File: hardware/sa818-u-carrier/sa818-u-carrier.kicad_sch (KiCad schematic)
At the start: 9 parts, among them J13 Conn_Coaxial, J14 Power/Audio, J15 Control/Data, J16 Conn_01x03_Pin, J17 Conn_01x03_Pin, U9 SA818V

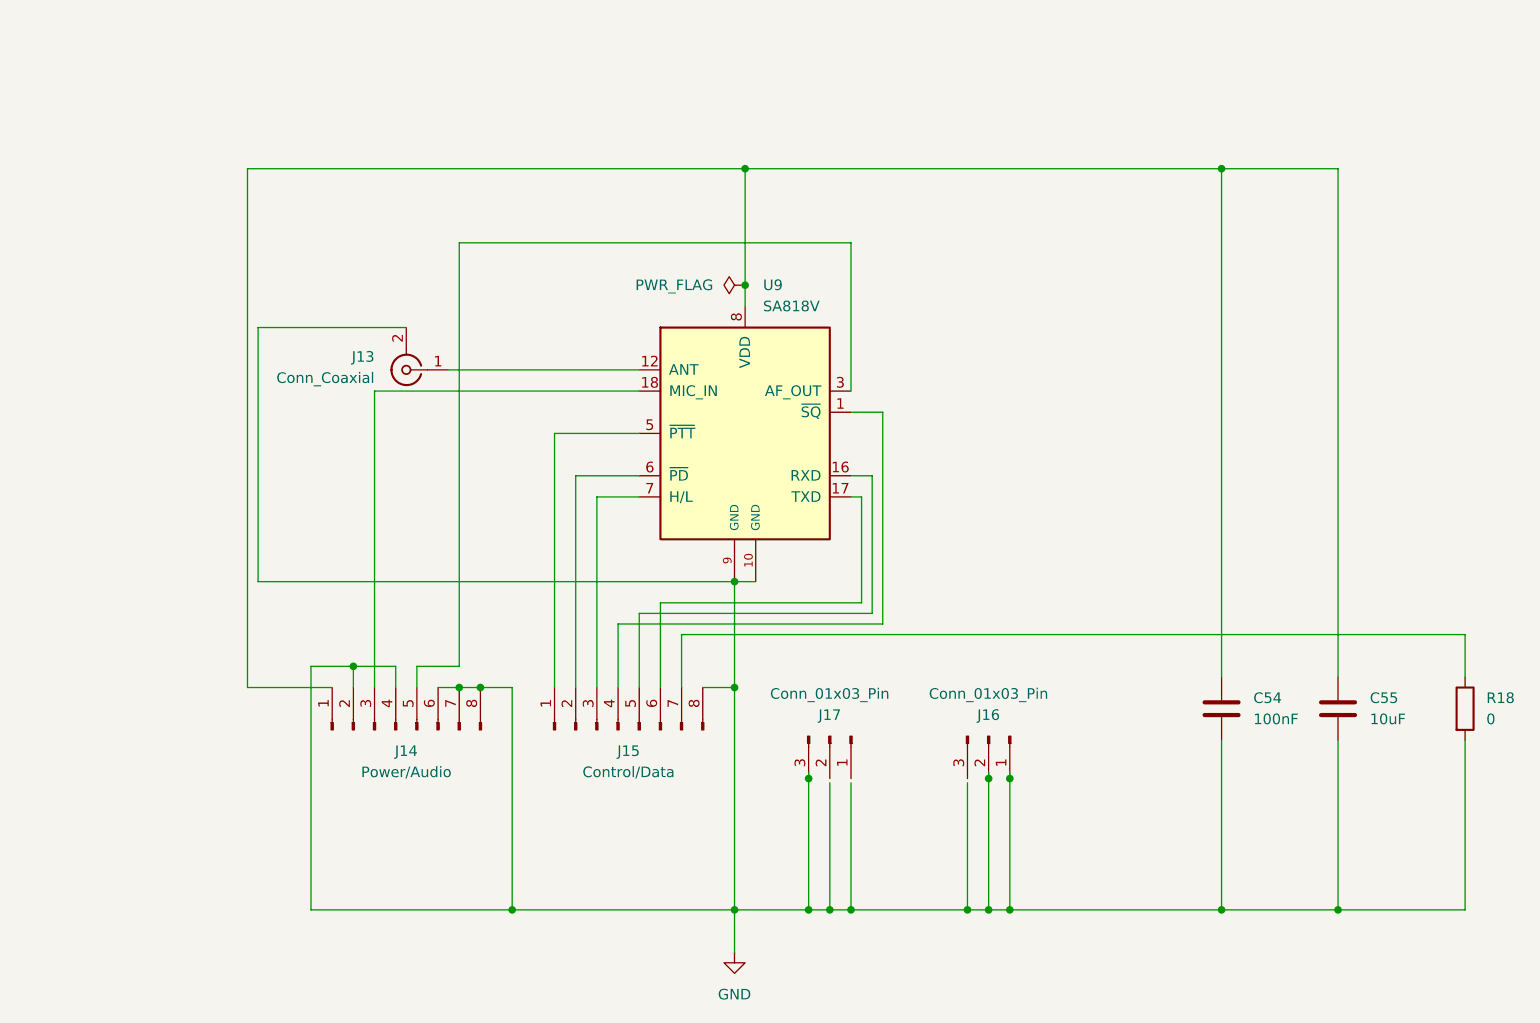
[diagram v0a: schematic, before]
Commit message: add footprints and break carrier boards out into standalone projects
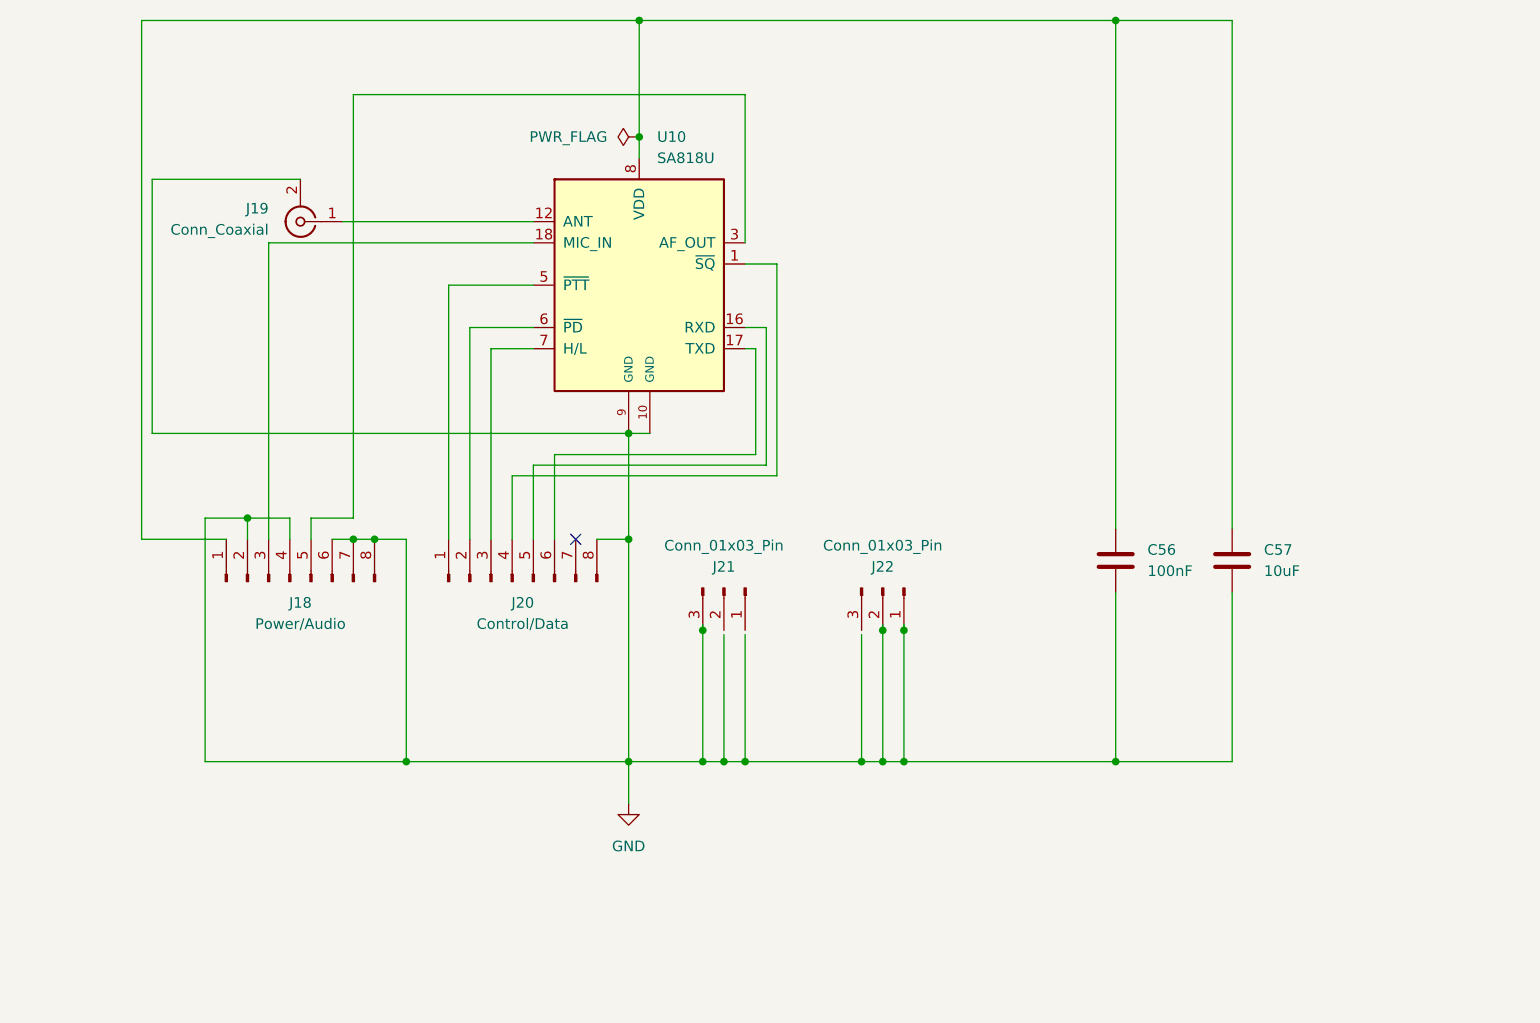
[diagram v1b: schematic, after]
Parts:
- removed C54: 100nF, Capacitor_SMD:C_0402_1005Metric, symbol Device:C
- removed C55: 10uF, Capacitor_SMD:C_0603_1608Metric, symbol Device:C
- removed J13: Conn_Coaxial, Connector_Coaxial:SMA_Amphenol_132289_EdgeMount, symbol Connector:Conn_Coaxial
- removed J14: Power/Audio, Connector_PinHeader_2.54mm:PinHeader_1x08_P2.54mm_Vertical, symbol Connector:Conn_01x08_Pin
- removed J15: Control/Data, Connector_PinHeader_2.54mm:PinHeader_1x08_P2.54mm_Vertical, symbol Connector:Conn_01x08_Pin
- removed J16, J17: Conn_01x03_Pin, Connector_PinHeader_2.54mm:PinHeader_1x03_P2.54mm_Vertical, symbol Connector:Conn_01x03_Pin
- removed R18: 0, Resistor_SMD:R_0402_1005Metric, symbol Device:R
- removed U9: SA818V, VHF_UHF_Modules:VHF_UHF_Module_generic, symbol VHF_UHF_Modules:SA818V
- added C56: 100nF, Capacitor_SMD:C_0402_1005Metric, symbol Device:C
- added C57: 10uF, Capacitor_SMD:C_0603_1608Metric, symbol Device:C
- added J18: Power/Audio, Connector_PinHeader_2.54mm:PinHeader_1x08_P2.54mm_Vertical, symbol Connector:Conn_01x08_Pin
- added J19: Conn_Coaxial, Connector_Coaxial:SMA_Amphenol_132289_EdgeMount, symbol Connector:Conn_Coaxial
- added J20: Control/Data, Connector_PinHeader_2.54mm:PinHeader_1x08_P2.54mm_Vertical, symbol Connector:Conn_01x08_Pin
- added J21, J22: Conn_01x03_Pin, Connector_PinHeader_2.54mm:PinHeader_1x03_P2.54mm_Vertical, symbol Connector:Conn_01x03_Pin
- added U10: SA818U, VHF_UHF_Modules:VHF_UHF_Module_generic, symbol VHF_UHF_Modules:SA818V
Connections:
- net GND: now also C56.2, C57.2, J18.2 (Pin_2), J18.4 (Pin_4), J18.6 (Pin_6), J18.7 (Pin_7), J18.8 (Pin_8), J19.2 (Ext), J20.8 (Pin_8), J21.3 (Pin_3), J22.1 (Pin_1), J22.2 (Pin_2), U10.10 (GND), U10.9 (GND)
- new net: J20.1 (Pin_1), U10.5 (~{PTT})
- new net: J20.2 (Pin_2), U10.6 (~{PD})
- new net: J20.3 (Pin_3), U10.7 (H/L)
- new net: J20.4 (Pin_4), U10.1 (~{SQ})
- new net: J20.5 (Pin_5), U10.16 (RXD)
- new net: J20.6 (Pin_6), U10.17 (TXD)
- new net: J19.1 (In), U10.12 (ANT)
- new net: J18.3 (Pin_3), U10.18 (MIC_IN)
- new net: J18.5 (Pin_5), U10.3 (AF_OUT)
- new net: C56.1, C57.1, J18.1 (Pin_1), U10.8 (VDD)
- no-connect marks 0 -> 1
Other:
- title: VHF RF Carrier Board -> UHF RF Carrier Board

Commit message: routing and component bug fixes
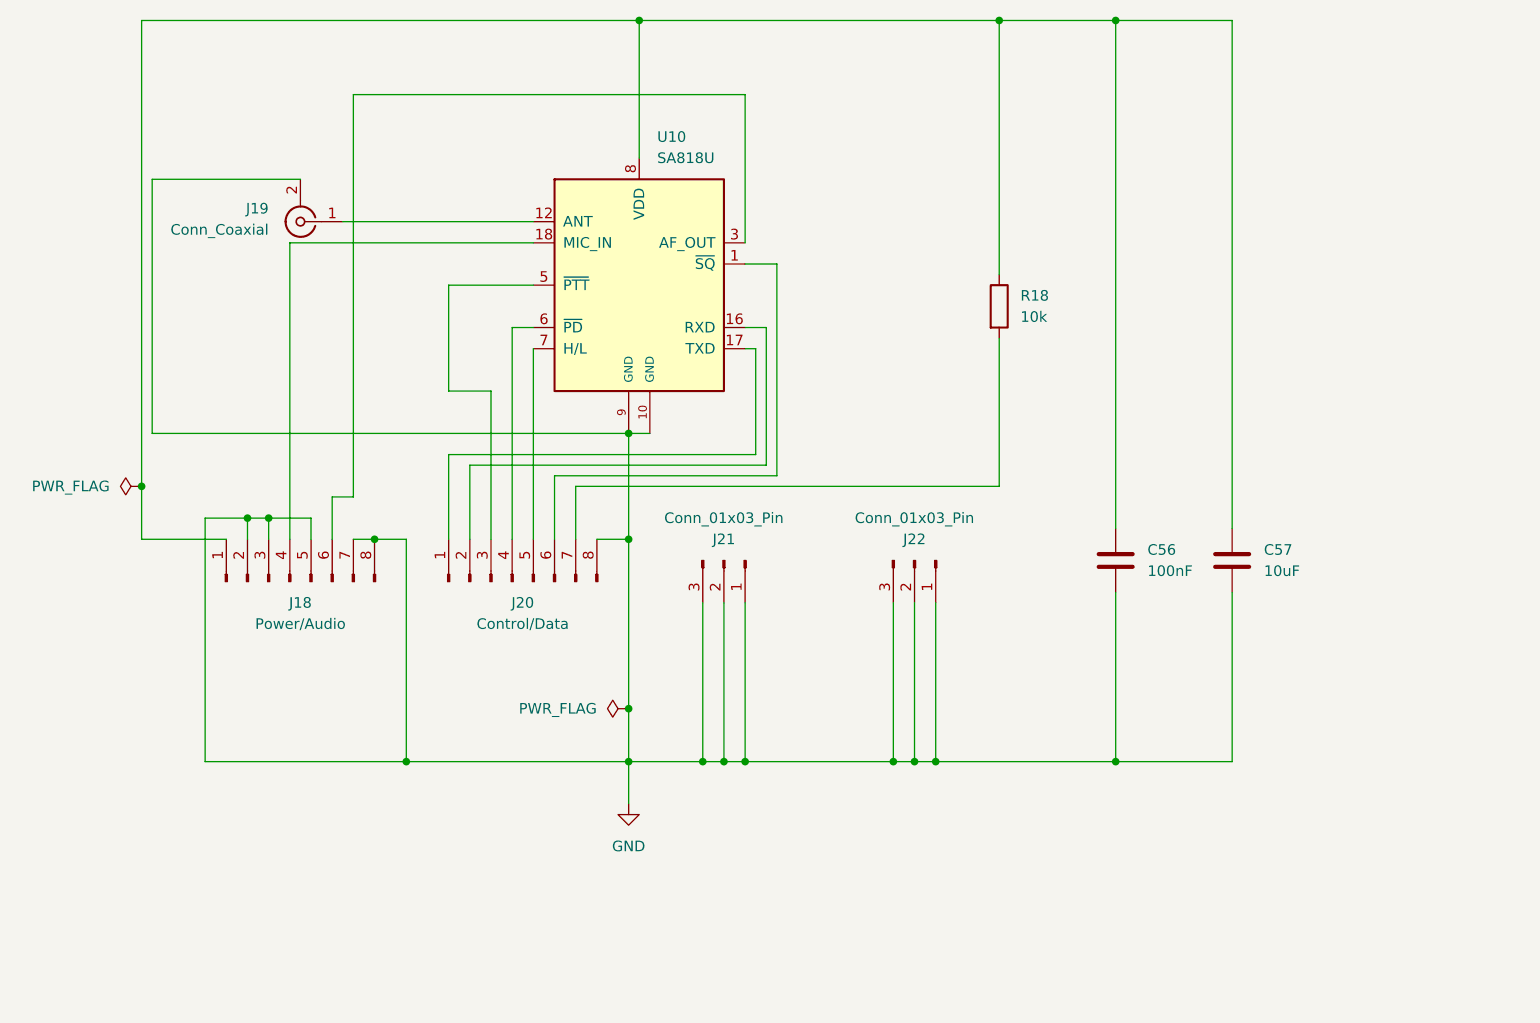
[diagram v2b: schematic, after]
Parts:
- added R18: 10k, Resistor_SMD:R_0402_1005Metric, symbol Device:R
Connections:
- net GND: now also J18.3 (Pin_3), J18.5 (Pin_5), J21.1 (Pin_1), J21.2 (Pin_2), J22.3 (Pin_3); no longer J18.4 (Pin_4), J18.6 (Pin_6)
- net at J20.1 (Pin_1): now also U10.17 (TXD); no longer U10.5 (~{PTT})
- net at J20.2 (Pin_2): now also U10.16 (RXD); no longer U10.6 (~{PD})
- net at J20.3 (Pin_3): now also U10.5 (~{PTT}); no longer U10.7 (H/L)
- net at J20.4 (Pin_4): now also U10.6 (~{PD}); no longer U10.1 (~{SQ})
- net at J20.5 (Pin_5): now also U10.7 (H/L); no longer U10.16 (RXD)
- net at J20.6 (Pin_6): now also U10.1 (~{SQ}); no longer U10.17 (TXD)
- net at J20.7 (Pin_7): now also R18.2
- net at U10.18 (MIC_IN): now also J18.4 (Pin_4); no longer J18.3 (Pin_3)
- net at U10.3 (AF_OUT): now also J18.6 (Pin_6); no longer J18.5 (Pin_5)
- net at C56.1, C57.1, J18.1 (Pin_1)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: now also R18.1
- no-connect marks 1 -> 0
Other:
- moved on the sheet: J21
